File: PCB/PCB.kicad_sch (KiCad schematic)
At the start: 0 parts

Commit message: Add ICs without configuration
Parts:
- added U1: INA219AxD, Package_SO:SOIC-8_3.9x4.9mm_P1.27mm, symbol Sensor_Energy:INA219AxD
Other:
- note added: "INA219 (SOIC-8)"
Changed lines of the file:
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@@
 		(comment 2 "Nyakallo Peete PTXNYA001")
+	)
+	(text "INA219 (SOIC-8)"
+		(exclude_from_sim no)
+		(at 25.4 17.526 0)
+		(effects
+			(font
+				(size 1.524 1.524)
+				(thickness 0.3048)
+				(bold yes)
+			)
+		)
+	)
+	(symbol
+		(lib_id "Sensor_Energy:INA219AxD")
+		(at 40.64 43.18 0)
+		(unit 1)
+		(exclude_from_sim no)
+		(in_bom yes)
+		(on_board yes)
+		(dnp no)
+		(fields_autoplaced yes)
+		(property "Reference" "U1"
+			(at 42.7833 30.48 0)
+			(effects
+				(font
+					(size 1.27 1.27)
+				)
+				(justify left)
+			)
+		)
+		(property "Value" "INA219AxD"
+			(at 42.7833 33.02 0)
+			(effects
+				(font
+					(size 1.27 1.27)
+				)
+				(justify left)
+			)
+		)
+		(property "Footprint" "Package_SO:SOIC-8_3.9x4.9mm_P1.27mm"
+			(at 60.96 52.07 0)
+			(effects
+				(font
+					(size 1.27 1.27)
+				)
+				(hide yes)
+			)
+		)
+		(property "Datasheet" "http://www.ti.com/lit/ds/symlink/ina219.pdf"
+			(at 49.53 45.72 0)
+			(effects
+				(font
+					(size 1.27 1.27)
+				)
+				(hide yes)
+			)
+		)
+		(property "Description" "Zero-Drift, Bidirectional Current/Power Monitor (0-26V) With I2C Interface, SOIC-8"
+			(at 40.64 43.18 0)
+			(effects
+				(font
+					(size 1.27 1.27)
+				)
+				(hide yes)
+			)
+		)
+		(pin "8"
+		)
+		(pin "4"
+		)
+		(pin "7"
+		)
+		(pin "5"
+		)
+		(pin "6"
+		)
+		(pin "3"
+		)
+		(pin "1"
+		)
+		(pin "2"
+		)
+		(instances
+			(project ""
+				(path "/0da9c021-1e1e-4699-b3a6-31bc4dd13bc3"
+					(reference "U1")
+					(unit 1)
+				)
+			)
+		)
 	)
 	(sheet_instances

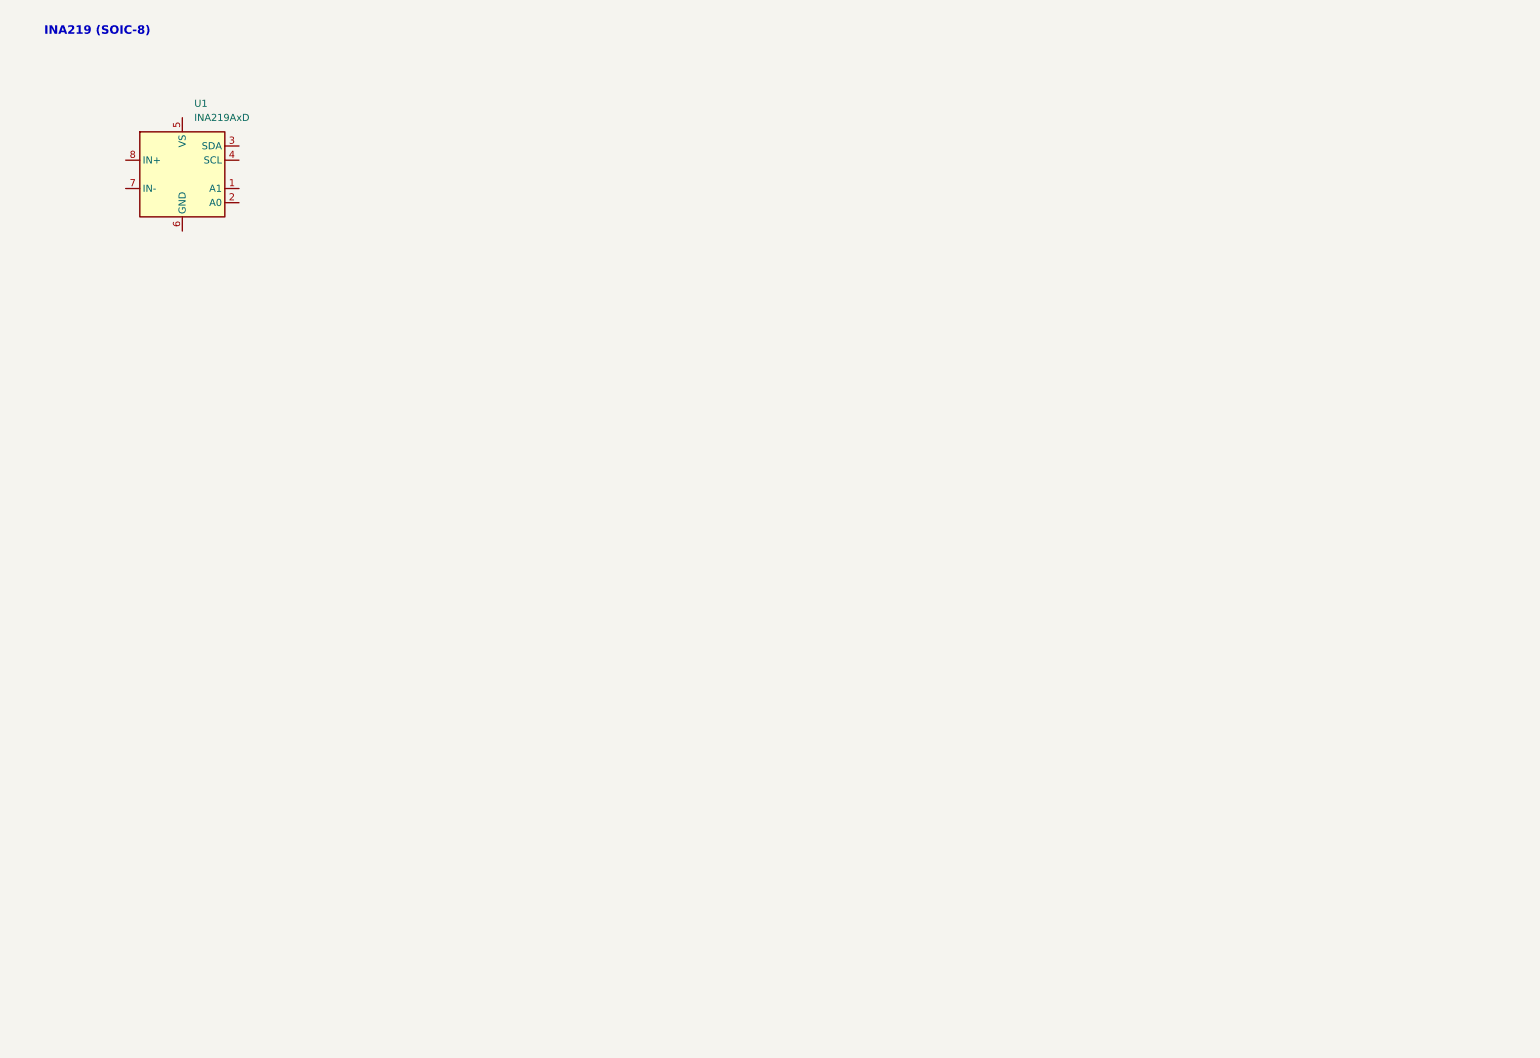
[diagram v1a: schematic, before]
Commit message: Pin Headers added with global labels
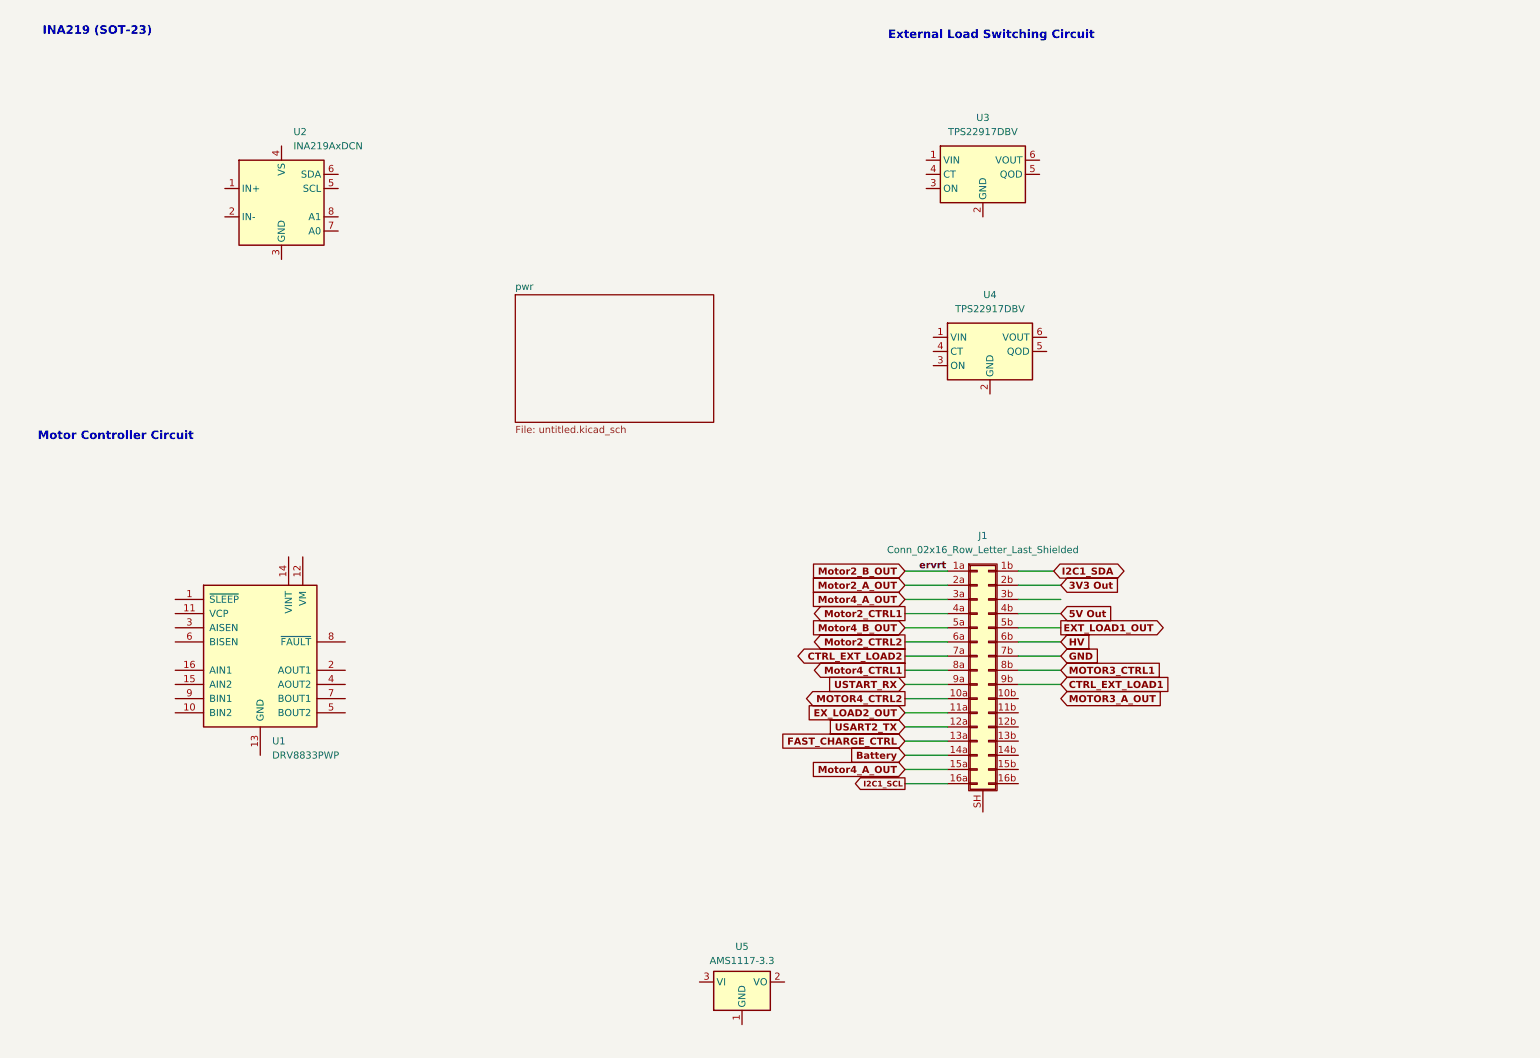
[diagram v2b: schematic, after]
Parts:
- removed U1: INA219AxD, Package_SO:SOIC-8_3.9x4.9mm_P1.27mm, symbol Sensor_Energy:INA219AxD
- added J1: Conn_02x16_Row_Letter_Last_Shielded, symbol Connector_Generic_Shielded:Conn_02x16_Row_Letter_Last_Shielded
- added U1: DRV8833PWP, Package_SO:HTSSOP-16-1EP_4.4x5mm_P0.65mm_EP3.4x5mm_Mask2.46x2.31mm_ThermalVias, symbol Driver_Motor:DRV8833PWP
- added U2: INA219AxDCN, Package_TO_SOT_SMD:SOT-23-8, symbol Sensor_Energy:INA219AxDCN
- added U3, U4: TPS22917DBV, Package_TO_SOT_SMD:SOT-23-6, symbol Power_Management:TPS22917DBV
- added U5: AMS1117-3.3, Package_TO_SOT_SMD:SOT-223-3_TabPin2, symbol Regulator_Linear:AMS1117-3.3
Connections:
- new net: U1.13 (GND), U1.17 (GND)
- new net 3V3 Out: J1.2b (Pin_2b)
- new net 5V Out: J1.4b (Pin_4b)
- new net Battery: J1.14a (Pin_14a)
- new net CTRL_EXT_LOAD1: J1.9b (Pin_9b)
- new net CTRL_EXT_LOAD2: J1.7a (Pin_7a)
- new net EXT_LOAD1_OUT: J1.5b (Pin_5b)
- new net EX_LOAD2_OUT: J1.11a (Pin_11a)
- new net FAST_CHARGE_CTRL: J1.13a (Pin_13a)
- new net GND: J1.7b (Pin_7b)
- new net HV: J1.6b (Pin_6b)
- new net I2C1_SCL: J1.16a (Pin_16a)
- new net I2C1_SDA: J1.1b (Pin_1b)
- new net MOTOR3_CTRL1: J1.8b (Pin_8b)
- new net MOTOR4_CTRL2: J1.10a (Pin_10a)
- new net Motor2_A_OUT: J1.2a (Pin_2a)
- new net Motor2_B_OUT: J1.1a (Pin_1a)
- new net Motor2_CTRL1: J1.4a (Pin_4a)
- new net Motor2_CTRL2: J1.6a (Pin_6a)
- new net Motor4_A_OUT: J1.15a (Pin_15a), J1.3a (Pin_3a)
- new net Motor4_B_OUT: J1.5a (Pin_5a)
- new net Motor4_CTRL1: J1.8a (Pin_8a)
- new net USART2_TX: J1.12a (Pin_12a)
- new net USTART_RX: J1.9a (Pin_9a)
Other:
- added sheet pwr (untitled.kicad_sch)
- note added: "External Load Switching Circuit"
- note added: "INA219 (SOT-23)"
- note added: "Motor Controller Circuit"
- note removed: "INA219 (SOIC-8)"

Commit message: Fix header labels and Add Charger IC
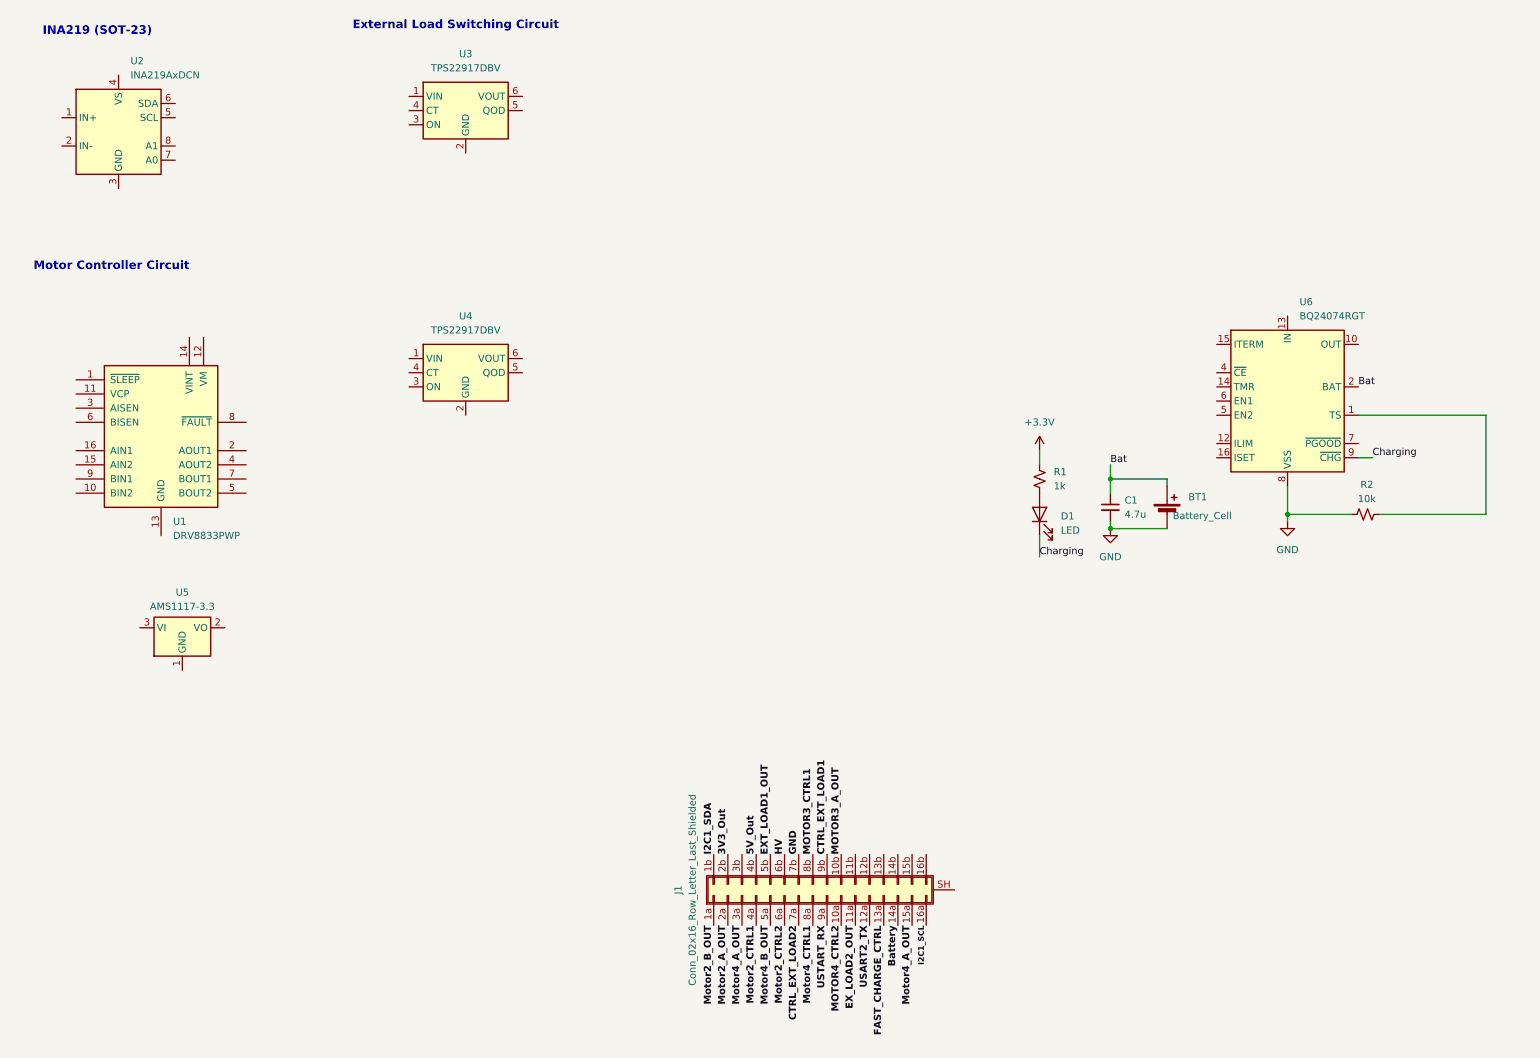
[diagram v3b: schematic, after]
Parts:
- added BT1: Battery_Cell, symbol Device:Battery_Cell
- added C1: 4.7u, symbol Device:C_Small
- added D1: LED, symbol Device:LED
- added R1: 1k, symbol Device:R_Small_US
- added R2: 10k, symbol Device:R_Small_US
- added U6: BQ24074RGT, Package_DFN_QFN:VQFN-16-1EP_3x3mm_P0.5mm_EP1.6x1.6mm, symbol Battery_Management:BQ24074RGT
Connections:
- net GND: now also BT1.2 (-), C1.2, R2.1, U6.17 (VSS), U6.8 (VSS)
- net MOTOR3_A_OUT: now also J1.10b (Pin_10b)
- net 3V3 Out renamed 3V3_Out
- net 5V Out renamed 5V_Out
- new net: D1.2 (A), R1.2
- new net: R2.2, U6.1 (TS)
- new net: U6.10 (OUT), U6.11 (OUT)
- new net +3.3V: R1.1
- new net Bat: BT1.1 (+), C1.1, U6.2 (BAT), U6.3 (BAT)
- new net Charging: D1.1 (K), U6.9 (~{CHG})
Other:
- removed sheet pwr
- moved on the sheet: J1, U1, U2, U3, U4, U5

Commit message: Semi configured schematic
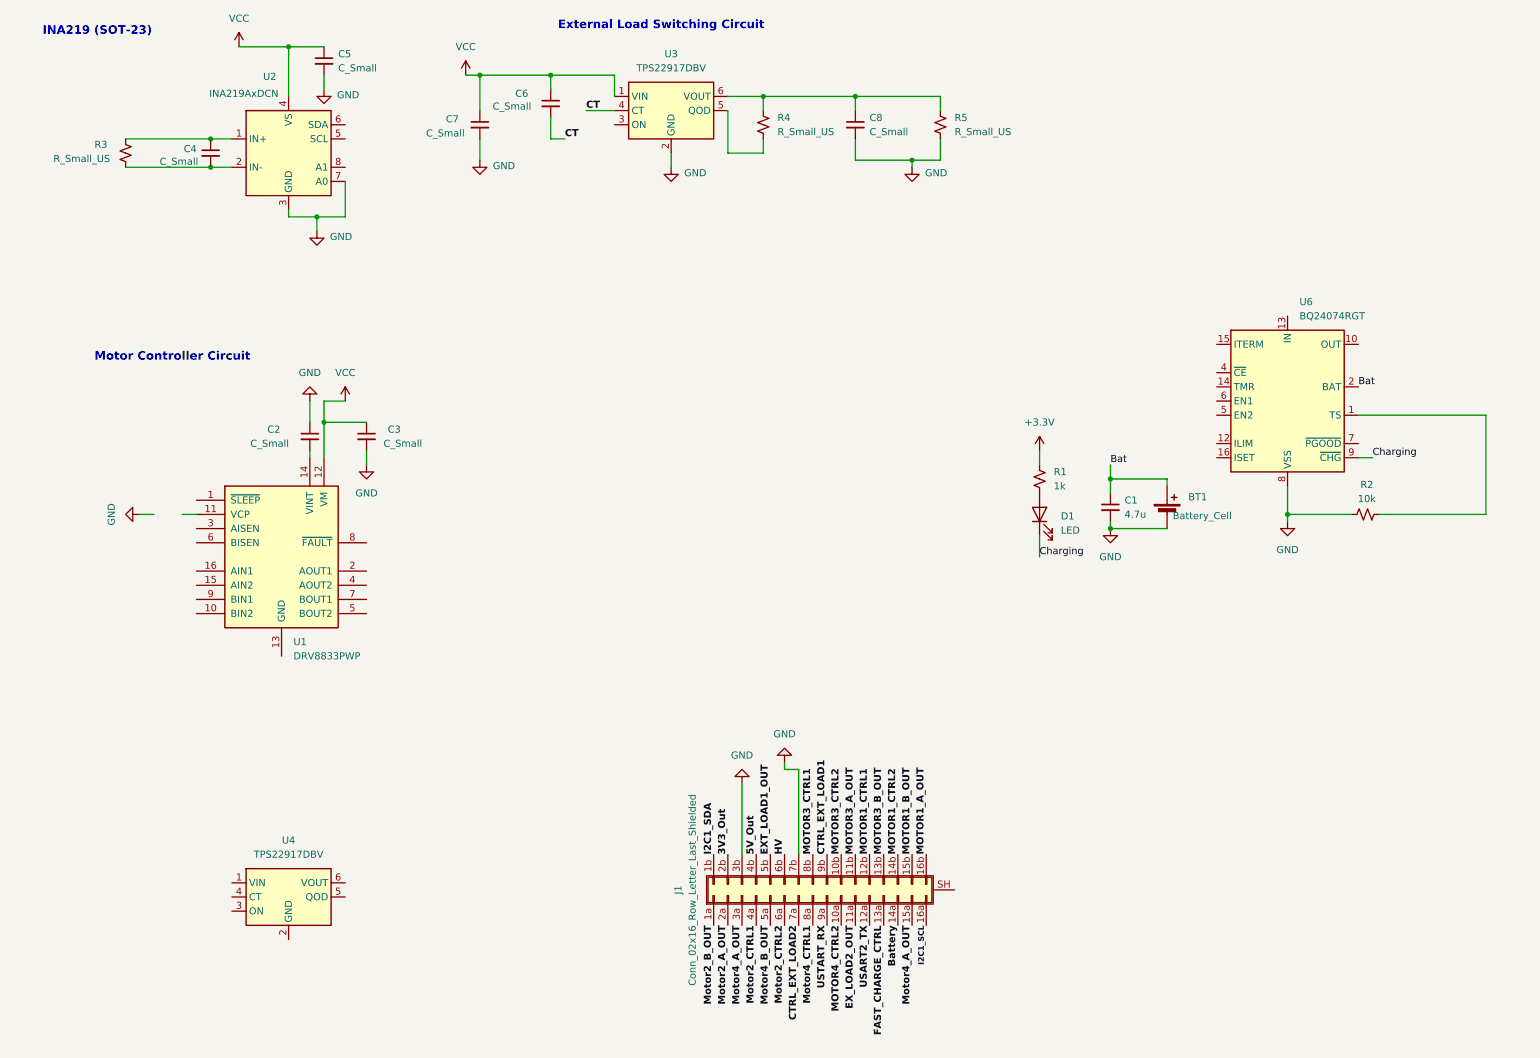
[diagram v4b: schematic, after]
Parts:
- removed U5: AMS1117-3.3, Package_TO_SOT_SMD:SOT-223-3_TabPin2, symbol Regulator_Linear:AMS1117-3.3
- added C2, C3, C4, C5, C6, C7, C8: C_Small, symbol Device:C_Small
- added R3, R4, R5: R_Small_US, symbol Device:R_Small_US
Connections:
- net GND: now also J1.3b (Pin_3b), U2.3 (GND), U2.7 (A0), U3.2 (GND), C2.1, C3.2, C5.2, C7.2, C8.2, R5.2
- net MOTOR3_A_OUT: now also J1.11b (Pin_11b); no longer J1.10b (Pin_10b)
- net VCC: now reaches U1.12 (VM)
- net VCC: now also U2.4 (VS), U3.1 (VIN), C3.1, C5.1, C6.1, C7.1
- net at U1.14 (VINT): now also C2.2
- net CT: now reaches U3.4 (CT)
- net CT: now also C6.2
- net at U3.5 (QOD): now also R4.2
- net at U3.6 (VOUT): now also C8.1, R4.1, R5.1
- net MOTOR1_CTRL1: now reaches J1.12b (Pin_12b)
- net MOTOR3_B_OUT: now reaches J1.13b (Pin_13b)
- net MOTOR1_CTRL2: now reaches J1.14b (Pin_14b)
- net MOTOR1_B_OUT: now reaches J1.15b (Pin_15b)
- net MOTOR1_A_OUT: now reaches J1.16b (Pin_16b)
- net at U2.1 (IN+): now also C4.1, R3.1
- net at U2.2 (IN-): now also C4.2, R3.2
- new net MOTOR3_CTRL2: J1.10b (Pin_10b)
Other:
- moved on the sheet: U1, U2, U3, U4
